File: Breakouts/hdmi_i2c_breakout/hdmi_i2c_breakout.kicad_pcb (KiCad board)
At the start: 2 copper layers, 30.1 x 20.8 mm, 14 parts, among them J1 ROW1, J2 ROW23, J3 AUX, J4 HDMI_A, Q1 Q_NMOS_GSD, Q2 Q_NMOS_GSD, SW1 SW_SPDT, U1 AP1117-33

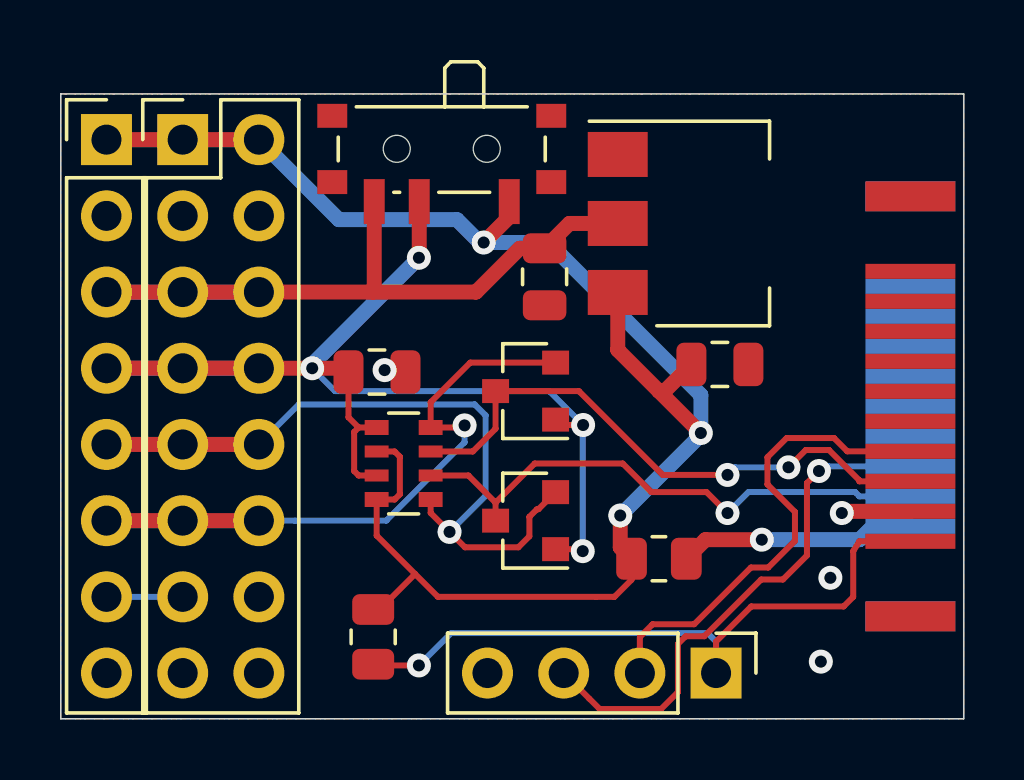
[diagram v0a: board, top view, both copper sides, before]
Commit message: Changed the HDMI plug in the Video I2C helper to correct pin numbering, rerouted traces to match, added shield connection to the SPDT switch symbol and pinout
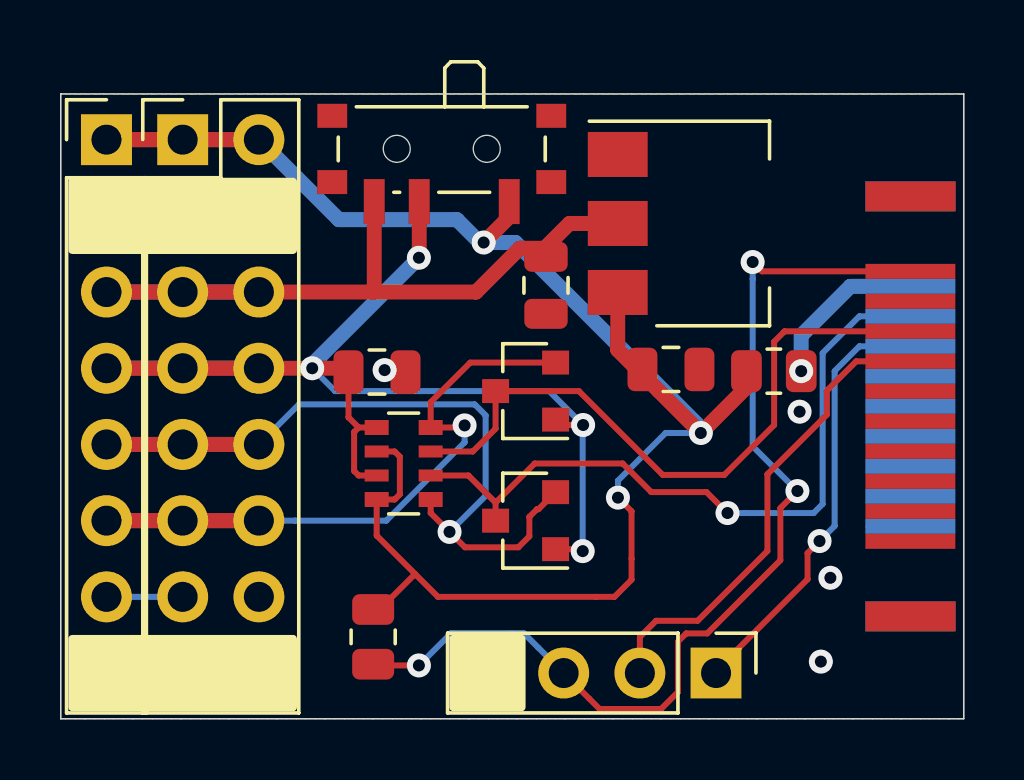
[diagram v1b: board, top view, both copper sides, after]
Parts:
- moved R2 7.33 mm to (149.2, 94.1)
- moved C2 1.64 mm to (145.8, 94.0)
- moved C1 0.29 mm to (141.7, 91.2)
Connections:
- J3 pad 1: HPD -> UTIL
- J3 pad 3: UTIL -> HPD
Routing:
- net HPD: track 22.9 -> 34.3 mm, vias 1 -> 3
- net SDA_5V: track 18.5 -> 23.9 mm
- net UTIL: track 17.9 -> 14.6 mm
- net SCL_5V: track 19.5 -> 22.3 mm, vias 2 -> 0
- net Net-(J4-Pad18): track 7.97 -> 5.51 mm
- net +5V: track 60.6 -> 62.0 mm
- net GND: track 3.03 -> 1.97 mm

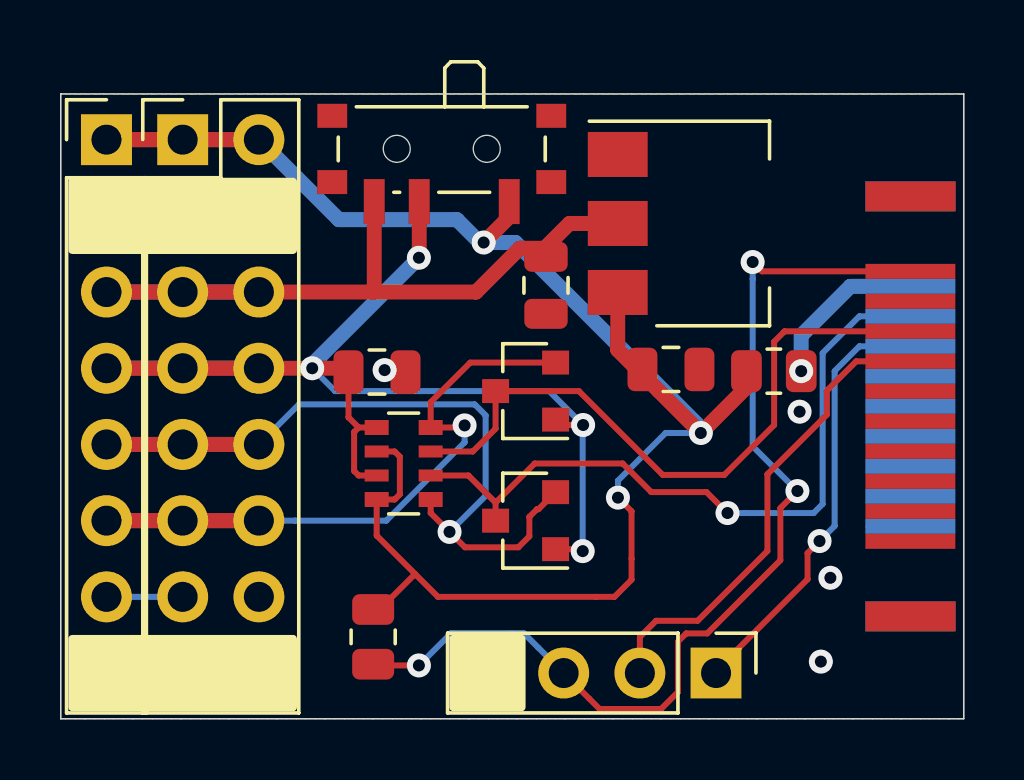
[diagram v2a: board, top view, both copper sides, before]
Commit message: Adding a power LED to the video I2C breakout, rerouting traces a bit to accomodate for that
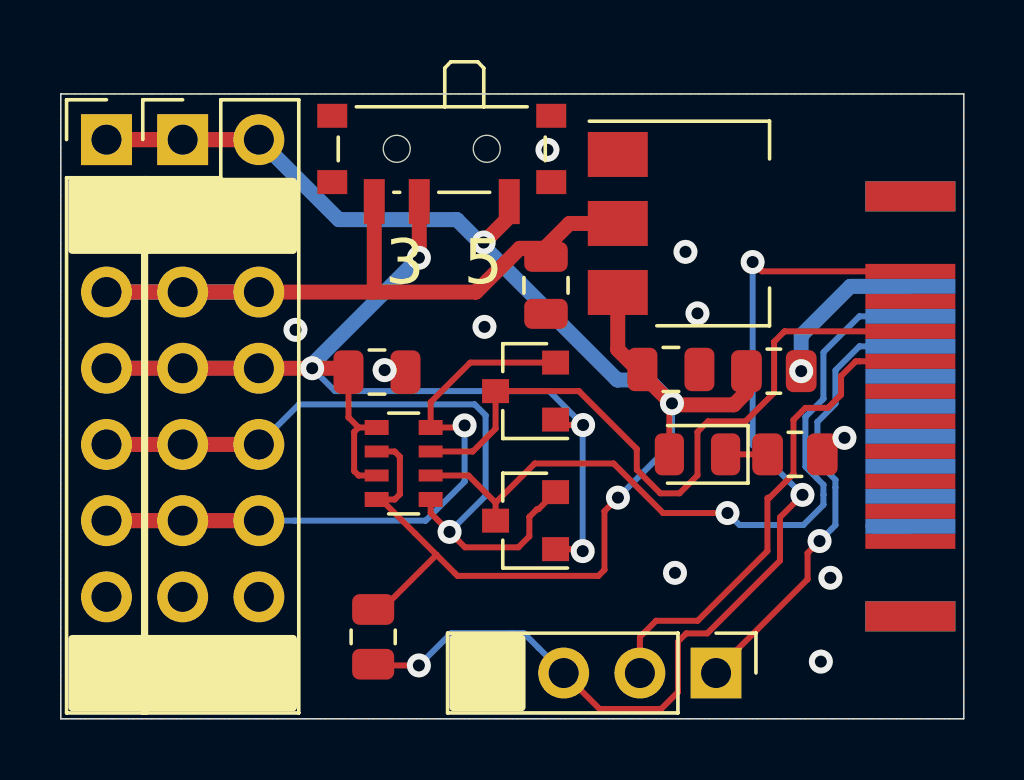
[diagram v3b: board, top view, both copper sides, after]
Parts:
- added D1: LED_Small, Diode_SMD:D_0805_2012Metric, F.Cu at (146.7, 96.8)
- added R3: 10K, Resistor_SMD:R_0805_2012Metric, F.Cu at (149.9, 96.8)
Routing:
- net Net-(J1-Pad7): track 2.54 -> 0.00 mm
- net +5V: track 62.0 -> 59.8 mm
- net Net-(D1-Pad1): track 0.00 -> 1.40 mm
- net SCL_5V: track 22.3 -> 23.5 mm
- net SDA_5V: track 23.9 -> 24.7 mm
- net SCL_SW: track 25.4 -> 26.1 mm
- net GND: vias 4 -> 10
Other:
- board text added: "3 5"

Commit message: Fixing small issue on the video I2C board, bumping it to v2
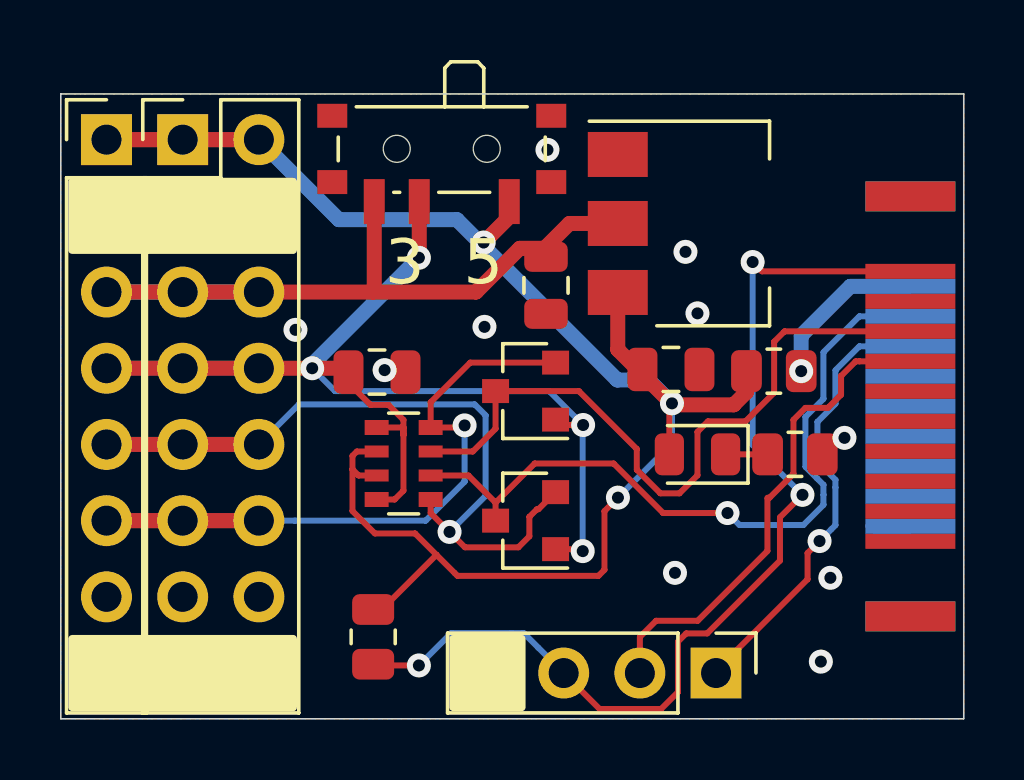
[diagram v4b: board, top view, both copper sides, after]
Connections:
- RN1 pad 3: +VSW -> +5V
- RN1 pad 4: +5V -> +VSW
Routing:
- net +VSW: track 41.1 -> 43.5 mm
- net +5V: track 59.8 -> 61.1 mm
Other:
- board text added: "Video I2C helper by CRImier, v2"
- board text removed: "Video I2C helper by CRImier, v1"
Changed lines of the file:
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@@
     (thickness 1.6)
     (drawings 8)
-    (tracks 224)
+    (tracks 229)
     (zones 0)
     (modules 16)
@@
   )
   (setup
-    (last_trace_width 0.2)
+    (last_trace_width 0.25)
     (user_trace_width 0.2)
     (user_trace_width 0.5)
@@
       (net 12 SCL_5V))
     (pad 4 smd rect (at -0.9 1.2) (size 0.8 0.5) (layers F.Cu F.Paste F.Mask)
-      (net 3 +5V))
+      (net 4 +VSW))
     (pad 2 smd rect (at -0.9 -0.4) (size 0.8 0.4) (layers F.Cu F.Paste F.Mask)
       (net 3 +5V))
     (pad 3 smd rect (at -0.9 0.4) (size 0.8 0.4) (layers F.Cu F.Paste F.Mask)
-      (net 4 +VSW))
+      (net 3 +5V))
     (pad 1 smd rect (at -0.9 -1.2) (size 0.8 0.5) (layers F.Cu F.Paste F.Mask)
       (net 4 +VSW))
@@
     (effects (font (size 1.5 1.5) (thickness 0.25)))
   )
-  (gr_text "Video I2C helper\nby CRImier, v1" (at 145.8595 91.7575 315) (layer B.SilkS)
+  (gr_text "Video I2C helper\nby CRImier, v2" (at 145.8595 91.7575 315) (layer B.SilkS)
     (effects (font (size 1 1) (thickness 0.15)) (justify mirror))
   )
@@
   (segment (start 135.89 91.44) (end 139.319 91.44) (width 0.5) (layer F.Cu) (net 2))
   (segment (start 132.08 91.44) (end 127 91.44) (width 0.5) (layer B.Cu) (net 2))
-  (segment (start 136.606 98.355) (end 136.006 98.355) (width 0.2) (layer F.Cu) (net 3))
-  (segment (start 136.779 98.182) (end 136.606 98.355) (width 0.2) (layer F.Cu) (net 3))
-  (segment (start 136.779 96.928) (end 136.779 98.182) (width 0.2) (layer F.Cu) (net 3))
-  (segment (start 136.606 96.755) (end 136.779 96.928) (width 0.2) (layer F.Cu) (net 3))
-  (segment (start 136.006 96.755) (end 136.606 96.755) (width 0.2) (layer F.Cu) (net 3))
   (segment (start 127 86.36) (end 129.54 86.36) (width 0.5) (layer F.Cu) (net 3))
   (segment (start 129.54 86.36) (end 132.08 86.36) (width 0.5) (layer F.Cu) (net 3))
@@
   (segment (start 147.909351 95.199989) (end 145.884305 95.199989) (width 0.5) (layer F.Cu) (net 3))
   (segment (start 145.884305 95.199989) (end 145.842158 95.157842) (width 0.5) (layer F.Cu) (net 3))
-  (segment (start 136.155 98.355) (end 136.006 98.355) (width 0.2) (layer F.Cu) (net 3))
-  (segment (start 137.287 99.487) (end 136.155 98.355) (width 0.2) (layer F.Cu) (net 3))
-  (segment (start 137.287 99.487) (end 138 100.2) (width 0.2) (layer F.Cu) (net 3))
   (segment (start 136.179 102.021) (end 135.89 102.021) (width 0.2) (layer F.Cu) (net 3))
   (segment (start 138 100.2) (end 136.179 102.021) (width 0.2) (layer F.Cu) (net 3))
@@
   (segment (start 138.6 100.8) (end 138 100.2) (width 0.2) (layer F.Cu) (net 3))
   (segment (start 144.04848 98.29292) (end 143.6 98.7414) (width 0.2) (layer F.Cu) (net 3))
-  (segment (start 135.406 97.555) (end 136.006 97.555) (width 0.2) (layer F.Cu) (net 4))
-  (segment (start 135.255 97.404) (end 135.406 97.555) (width 0.2) (layer F.Cu) (net 4))
-  (segment (start 135.255 96.106) (end 135.255 97.404) (width 0.2) (layer F.Cu) (net 4))
-  (segment (start 135.406 95.955) (end 135.255 96.106) (width 0.2) (layer F.Cu) (net 4))
-  (segment (start 136.006 95.955) (end 135.406 95.955) (width 0.2) (layer F.Cu) (net 4))
+  (segment (start 135.406 97.555) (end 135.2 97.349) (width 0.2) (layer F.Cu) (net 3))
+  (segment (start 136.006 97.555) (end 135.406 97.555) (width 0.2) (layer F.Cu) (net 3))
+  (segment (start 135.2 97.349) (end 135.2 96.9) (width 0.2) (layer F.Cu) (net 3))
+  (segment (start 135.345 96.755) (end 136.006 96.755) (width 0.2) (layer F.Cu) (net 3))
+  (segment (start 135.2 96.9) (end 135.345 96.755) (width 0.2) (layer F.Cu) (net 3))
+  (segment (start 135.2 98.739002) (end 135.2 97.349) (width 0.2) (layer F.Cu) (net 3))
+  (segment (start 135.947998 99.487) (end 135.2 98.739002) (width 0.2) (layer F.Cu) (net 3))
+  (segment (start 137.287 99.487) (end 135.947998 99.487) (width 0.2) (layer F.Cu) (net 3))
+  (segment (start 138 100.2) (end 137.287 99.487) (width 0.2) (layer F.Cu) (net 3))
+  (segment (start 136.155 98.355) (end 136.006 98.355) (width 0.2) (layer F.Cu) (net 4))
   (segment (start 132.08 93.98) (end 129.54 93.98) (width 0.5) (layer F.Cu) (net 4))
   (segment (start 127 93.98) (end 129.54 93.98) (width 0.5) (layer F.Cu) (net 4))
   (segment (start 134.94 93.98) (end 135.067 94.107) (width 0.5) (layer F.Cu) (net 4))
-  (segment (start 135.067 95.616) (end 135.067 94.107) (width 0.2) (layer F.Cu) (net 4))
-  (segment (start 135.406 95.955) (end 135.067 95.616) (width 0.2) (layer F.Cu) (net 4))
   (via (at 142.875 100.076) (size 0.8) (drill 0.4) (layers F.Cu B.Cu) (net 4))
   (segment (start 142.809 100.01) (end 142.875 100.076) (width 0.2) (layer F.Cu) (net 4))
@@
   (segment (start 137.414 90.297) (end 133.858 93.853) (width 0.5) (layer B.Cu) (net 4))
   (segment (start 127 93.98) (end 132.08 93.98) (width 0.5) (layer B.Cu) (net 4))
+  (segment (start 136.606 98.355) (end 136.9 98.061) (width 0.2) (layer F.Cu) (net 4))
+  (segment (start 136.006 98.355) (end 136.606 98.355) (width 0.2) (layer F.Cu) (net 4))
+  (segment (start 136.9 98.061) (end 136.9 96.2) (width 0.2) (layer F.Cu) (net 4))
+  (segment (start 135.067 94.467) (end 135.067 94.107) (width 0.2) (layer F.Cu) (net 4))
+  (segment (start 135.8 95.2) (end 135.067 94.467) (width 0.2) (layer F.Cu) (net 4))
+  (segment (start 136.4 95.2) (end 135.8 95.2) (width 0.2) (layer F.Cu) (net 4))
+  (segment (start 136.9 95.7) (end 136.4 95.2) (width 0.2) (layer F.Cu) (net 4))
+  (segment (start 136.9 96.2) (end 136.9 95.7) (width 0.2) (layer F.Cu) (net 4))
+  (segment (start 136.9 95.955) (end 136.006 95.955) (width 0.2) (layer F.Cu) (net 4))
+  (segment (start 136.9 96.2) (end 136.9 95.955) (width 0.2) (layer F.Cu) (net 4))
   (segment (start 137.806 95.112) (end 137.806 95.955) (width 0.2) (layer F.Cu) (net 6))
   (segment (start 139.126 93.792) (end 137.806 95.112) (width 0.2) (layer F.Cu) (net 6))

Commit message: video_i2c_breakout: v2, functional changes
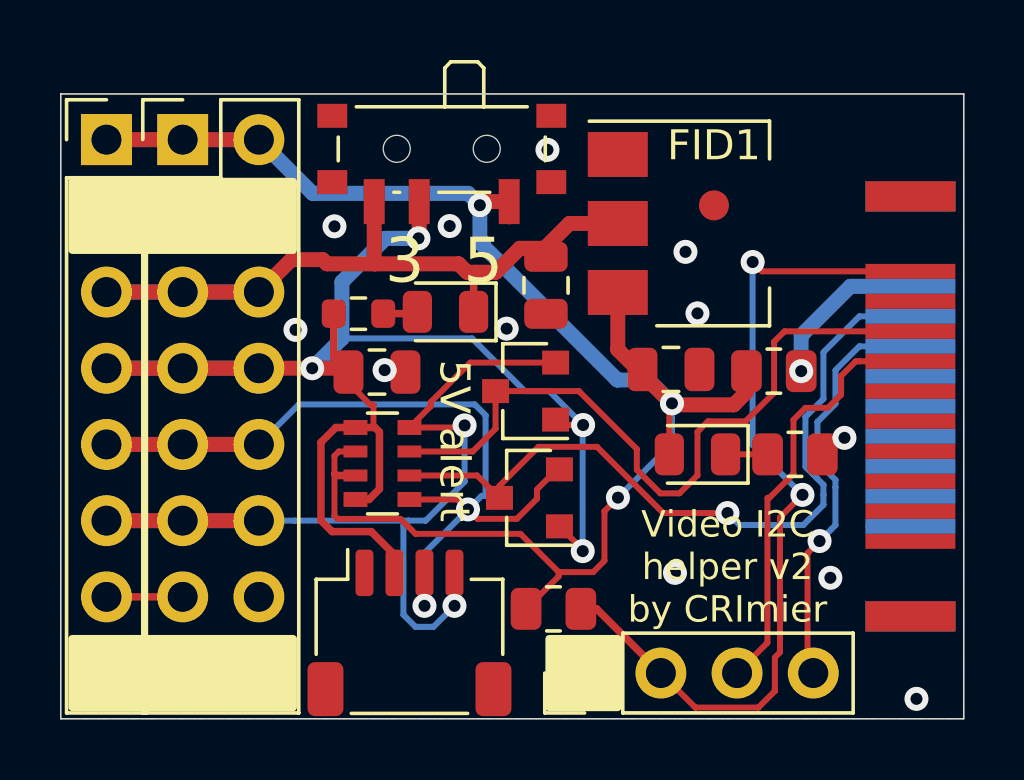
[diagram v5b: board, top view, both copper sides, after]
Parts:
- added D2: 5V_ALRT, Diode_SMD:D_0805_2012Metric, F.Cu at (138.3, 92.1)
- added FID1: Fiducial, Fiducial:Fiducial_1mm_Mask2mm, F.Cu at (147.2, 88.5)
- added J5: QWIIC, Connector_JST:JST_SH_SM04B-SRSS-TB_1x04-1MP_P1.00mm_Horizontal, F.Cu at (137.1, 102.8)
- added R4: 120R, Resistor_SMD:R_0603_1608Metric, F.Cu at (135.4, 92.2)
- moved R1 6.08 mm to (141.9, 102.0), turned to 0 degrees
- moved J3 4.38 mm to (142.9, 104.1), turned to 90 degrees
- moved Q2 0.77 mm to (141.1, 98.3)
- moved RN1 0.71 mm to (136.2, 97.2)
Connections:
- J1 pad 7: Net-(J1-Pad7) -> unconnected-(J1-Pad7)
- J2 pad 13: Net-(J1-Pad7) -> unconnected-(J1-Pad7)
- J2 pad 14: Net-(J2-Pad14) -> unconnected-(J2-Pad14)
- J3 pad 1: UTIL -> GND
- J3 pad 2: CEC -> HPD
- J3 pad 3: HPD -> CEC
- J3 pad 4: GND -> UTIL
- J4 pad 1: Net-(J4-Pad1) -> unconnected-(J4-Pad1)
- J4 pad 10: Net-(J4-Pad10) -> unconnected-(J4-Pad10)
- J4 pad 12: Net-(J4-Pad12) -> unconnected-(J4-Pad12)
- J4 pad 3: Net-(J4-Pad3) -> unconnected-(J4-Pad3)
- J4 pad 4: Net-(J4-Pad4) -> unconnected-(J4-Pad4)
- J4 pad 6: Net-(J4-Pad6) -> unconnected-(J4-Pad6)
- J4 pad 7: Net-(J4-Pad7) -> unconnected-(J4-Pad7)
- J4 pad 9: Net-(J4-Pad9) -> unconnected-(J4-Pad9)
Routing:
- net +VSW: track 43.5 -> 52.1 mm
- net SCL_SW: track 26.1 -> 33.6 mm, vias 1 -> 2
- net HPD: track 34.4 -> 28.8 mm, vias 3 -> 2
- net SDA_SW: track 29.0 -> 32.9 mm, vias 1 -> 2
- net unconnected-(J1-Pad7): track 0.00 -> 2.54 mm
- net CEC: track 16.4 -> 14.4 mm
- net UTIL: track 15.1 -> 13.9 mm
- net Net-(D2-Pad2): track 0.00 -> 1.16 mm
- net +3V3: track 26.1 -> 26.9 mm
- net SCL_5V: track 23.5 -> 24.2 mm
- net SDA_5V: track 24.7 -> 25.4 mm
- net GND: vias 10 -> 12
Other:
- net class Default removed
- board text added: "+5V GND +3.3V VSW SDA SCL x G"
- board text added: "5V alert"
- board text added: "VSW = 5V or 3.3V, depending on switch"
- board text added: "Video I2C helper v2 by CRImier"
- board text added: "gnd vsw sda scl"
- board text added: "qwiic"
- board text removed: "+5V GND +3.3V VSW SDA SCL NC GND"
